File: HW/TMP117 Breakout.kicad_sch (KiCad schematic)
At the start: 6 parts, among them J1 IO, U1 TMP117xxDRV

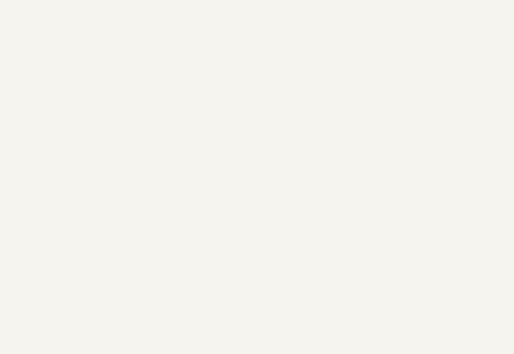
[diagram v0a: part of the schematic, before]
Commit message: Completed layout
- Completed PCB layout and routing
- Plotted GERBER files
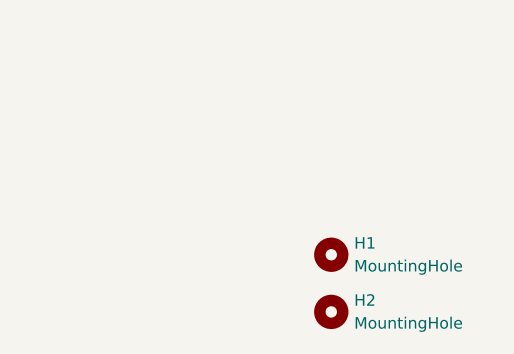
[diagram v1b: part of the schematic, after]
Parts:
- added H1, H2: MountingHole, MountingHole:MountingHole_3.2mm_M3_Pad_Via, symbol Mechanical:MountingHole
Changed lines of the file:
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@@
+    )
+  )
+  (symbol (lib_id "Mechanical:MountingHole") (at 156.21 170.18 0) (unit 1)
+    (in_bom yes) (on_board yes) (dnp no)
+    (property "Reference" "H1" (at 158.75 168.91 0)
+      (effects (font (size 1.27 1.27)) (justify left))
+    )
+    (property "Value" "MountingHole" (at 158.75 171.45 0)
+      (effects (font (size 1.27 1.27)) (justify left))
+    )
+    (property "Footprint" "MountingHole:MountingHole_3.2mm_M3_Pad_Via" (at 156.21 170.18 0)
+      (effects (font (size 1.27 1.27)) hide)
+    )
+    (property "Datasheet" "~" (at 156.21 170.18 0)
+      (effects (font (size 1.27 1.27)) hide)
+    )
+    (instances
+      (project "TMP117 Breakout"
+        (path "/8e88e8ac-f1b3-4d96-ab24-388c44d4af4e"
+          (reference "H1") (unit 1)
+        )
+      )
     )
   )
@@
     )
   )
+  (symbol (lib_id "Mechanical:MountingHole") (at 156.21 176.53 0) (unit 1)
+    (in_bom yes) (on_board yes) (dnp no)
+    (property "Reference" "H2" (at 158.75 175.26 0)
+      (effects (font (size 1.27 1.27)) (justify left))
+    )
+    (property "Value" "MountingHole" (at 158.75 177.8 0)
+      (effects (font (size 1.27 1.27)) (justify left))
+    )
+    (property "Footprint" "MountingHole:MountingHole_3.2mm_M3_Pad_Via" (at 156.21 176.53 0)
+      (effects (font (size 1.27 1.27)) hide)
+    )
+    (property "Datasheet" "~" (at 156.21 176.53 0)
+      (effects (font (size 1.27 1.27)) hide)
+    )
+    (instances
+      (project "TMP117 Breakout"
+        (path "/8e88e8ac-f1b3-4d96-ab24-388c44d4af4e"
+          (reference "H2") (unit 1)
+        )
+      )
+    )
+  )
   (symbol (lib_id "power:GND") (at 143.51 110.49 0) (unit 1)
     (in_bom yes) (on_board yes) (dnp no) (fields_autoplaced)
@@
       (effects (font (size 1.27 1.27)) (justify left) hide)
     )
-    (pin "7")
     (pin "1")
     (pin "2")
@@
     (pin "5")
     (pin "6")
-    (instances
-      (project "TMP117 Breakout"
+    (pin "7")
+    (instances
+      (project "TMP117 Breakout"
